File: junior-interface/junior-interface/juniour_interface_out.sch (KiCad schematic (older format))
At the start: 9 parts, among them IC6 NE565, IC7 LM311, IC8 LM311, J3 DB25_Female, T1 BC547

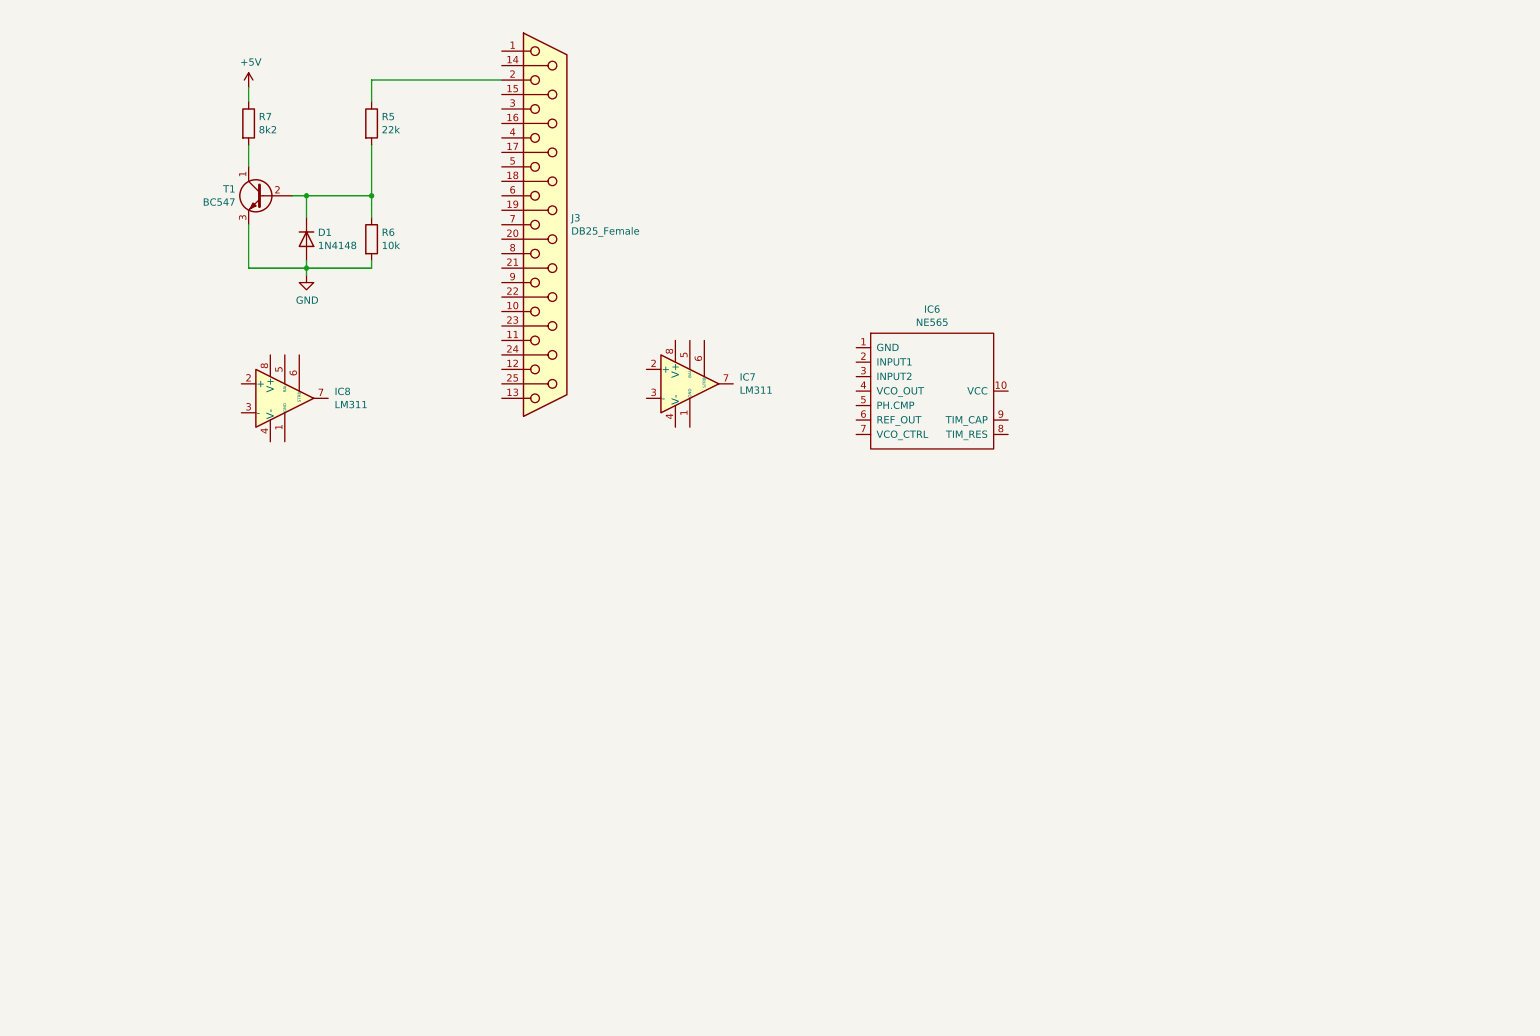
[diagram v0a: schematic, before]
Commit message: junior interface schema
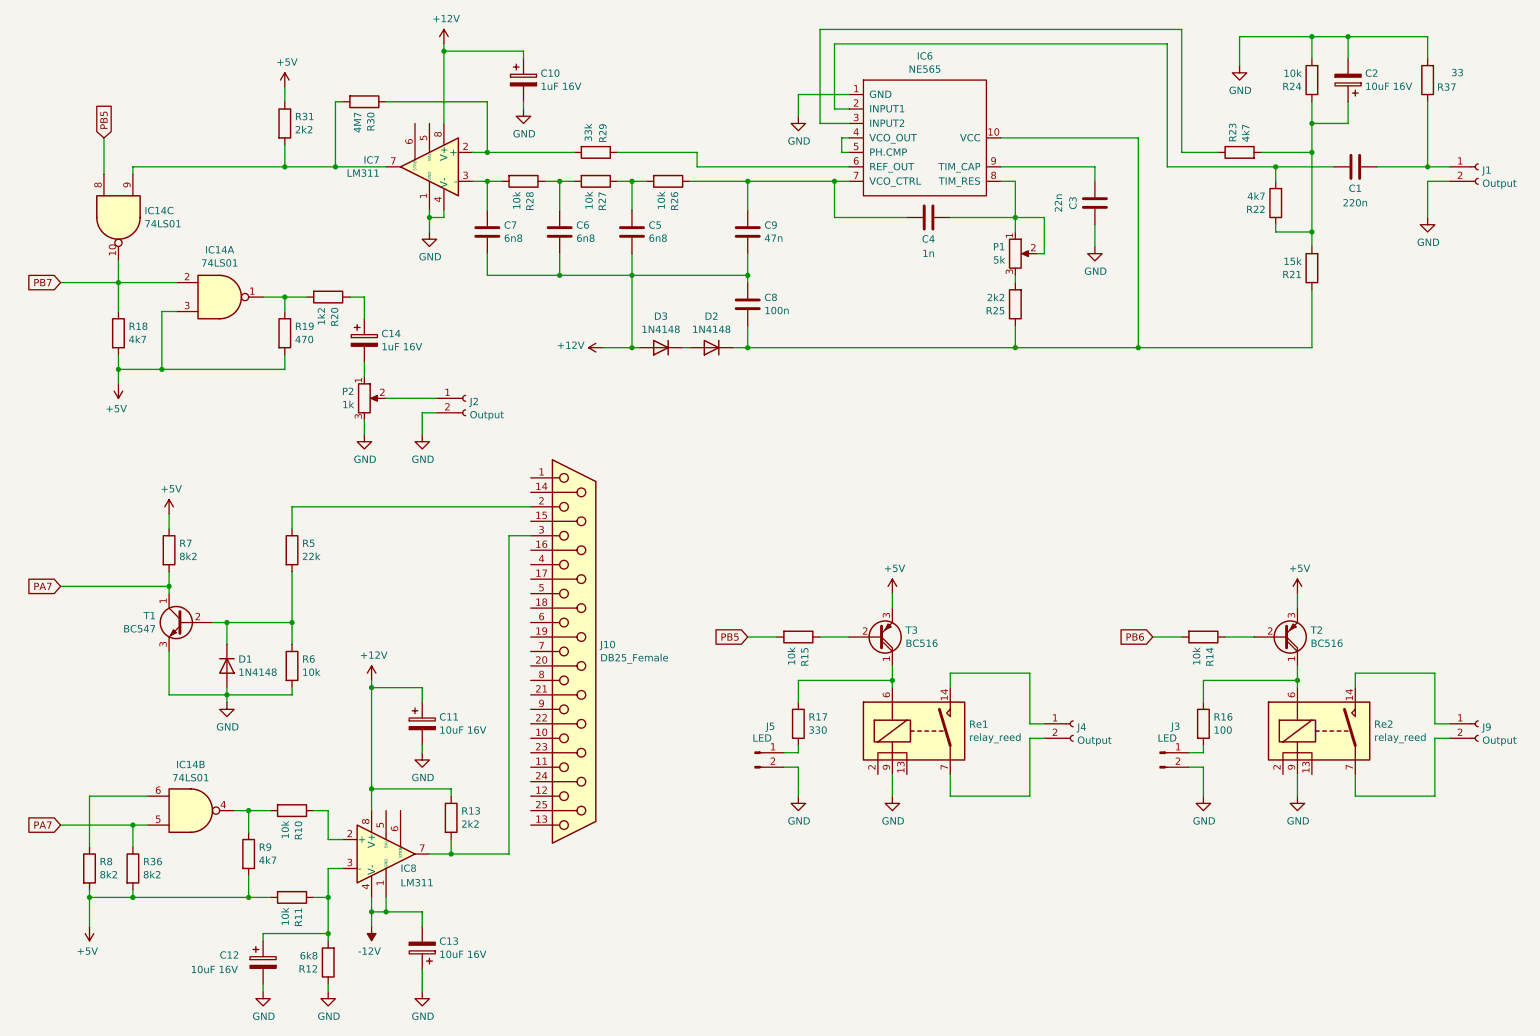
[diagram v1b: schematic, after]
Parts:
- added C1: 220n, elektor:CAP-3, symbol Device:C
- added C10, C14: 1uF 16V, elektor:CAP-POL-3, symbol Device:CP
- added C11, C12, C13, C2: 10uF 16V, elektor:CAP-POL-3, symbol Device:CP
- added C3: 22n, elektor:CAP-3, symbol Device:C
- added C4: 1n, elektor:CAP-3, symbol Device:C
- added C5, C6, C7: 6n8, elektor:CAP-3, symbol Device:C
- added C8: 100n, elektor:CAP-3, symbol Device:C
- added C9: 47n, elektor:CAP-3, symbol Device:C
- added D2, D3: 1N4148, elektor:Diod-4, symbol Device:D
- added IC14: 74LS01, symbol 74xx:74LS01
- added J1, J2, J4, J9: Output, elektor:RCA_CI, symbol Connector:Conn_01x02_Female
- added J3, J5: LED, symbol Connector:Conn_01x02_Male
- added P1: 5k, Potentiometers:Potentiometer_Trimmer_Bourns_3005, symbol Device:R_POT
- added P2: 1k, Potentiometers:Potentiometer_Trimmer_ACP_CA9v_Horizontal_Px10.0mm_Py5.0mm, symbol Device:R_POT
- added R10, R11, R14, R15, R24, R26, R27, R28: 10k, elektor:Res-5, symbol Device:R
- added R12: 6k8, elektor:Res-5, symbol Device:R
- added R13, R25, R31: 2k2, elektor:Res-5, symbol Device:R
- added R16: 100, elektor:Res-5, symbol Device:R
- added R17: 330, elektor:Res-5, symbol Device:R
- added R18, R22, R23, R9: 4k7, elektor:Res-5, symbol Device:R
- added R19: 470, elektor:Res-5, symbol Device:R
- added R20: 1k2, elektor:Res-5, symbol Device:R
- added R21: 15k, elektor:Res-5, symbol Device:R
- added R29: 33k, elektor:Res-5, symbol Device:R
- added R30: 4M7, elektor:Res-5, symbol Device:R
- added R36, R8: 8k2, elektor:Res-5, symbol Device:R
- added R37: 33, elektor:Res-5, symbol Device:R
- added Re1, Re2: relay_reed, elektor:DIL-14, symbol junior_computer:relay_reed
- added T2, T3: BC516, TO_SOT_Packages_THT:TO-92_Molded_Wide, symbol Transistor_BJT:BC516
- J10: renamed from J3; footprint (none) -> elektor:DB25-F-CI
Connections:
- net +5V: now also IC14.3, R11.2, R18.2, R19.2, R31.1, R36.2, R8.2, R9.2, T2.3 (E), T3.3 (E)
- net GND: now also IC6.1 (GND), IC7.1 (GND), IC7.4 (V-), C10.2, C11.2, C12.2, C13.1, C2.2, C3.2, J1.2 (Pin_2), J2.2 (Pin_2), J3.2 (Pin_2), J5.2 (Pin_2), P2.3, R12.1, R24.2, R37.2, Re1.9, Re2.9
- net at IC7.2 (+): now also R29.2, R30.1
- net at IC7.3 (-): now also C7.1, R28.2
- net at IC7.7: now also IC14.9, R30.2, R31.2
- net +12V: now reaches IC7.8 (V+)
- net +12V: now also IC8.8 (V+), C10.1, C11.1, C5.2, C6.2, C7.2, C8.1, C9.2, D3.2 (A), R13.1
- net -12V: now reaches IC8.1 (GND)
- net -12V: now also IC8.4 (V-), C13.2
- net at IC8.2 (+): now also R10.1
- net at IC8.3 (-): now also C12.1, R11.1, R12.2
- net at IC8.7: now also J10.3, R13.2
- net at IC6.10 (VCC): now also C8.2, D2.1 (K), R21.1, R25.1
- net at IC6.2 (INPUT1): now also C1.1, R22.2
- net at IC6.3 (INPUT2): now also R23.1
- net at IC6.4 (VCO_OUT): now also IC6.5 (PH.CMP)
- net at IC6.6 (REF_OUT): now also R29.1
- net at IC6.7 (VCO_CTRL): now also C4.1, C9.1, R26.1
- net at IC6.8 (TIM_RES): now also C4.2, P1.1, P1.2
- net at IC6.9 (TIM_CAP): now also C3.1
- net PA7: now reaches R7.2, T1.1 (C)
- net PA7: now also IC14.5, R36.1
- new net: IC14.4, R10.2, R9.1
- new net: IC14.6, R8.1
- new net: R17.1, Re1.6, T3.1 (C)
- new net: R15.1, T3.2 (B)
- new net: J4.1 (Pin_1), Re1.14
- new net: J4.2 (Pin_2), Re1.7
- new net: J5.1 (Pin_1), R17.2
- new net: R16.1, Re2.6, T2.1 (C)
- new net: R14.1, T2.2 (B)
- new net: J9.1 (Pin_1), Re2.14
- new net: J9.2 (Pin_2), Re2.7
- new net: J3.1 (Pin_1), R16.2
- new net: IC14.1, R19.1, R20.2
- new net: C14.1, R20.1
- new net: C14.2, P2.1
- new net: J2.1 (Pin_1), P2.2
- new net: C6.1, R27.2, R28.1
- new net: C5.1, R26.2, R27.1
- new net: D2.2 (A), D3.1 (K)
- new net: P1.3, R25.2
- new net: C2.1, R21.2, R22.1, R23.2, R24.1
- new net: C1.2, J1.1 (Pin_1), R37.1
- new net PB5: IC14.8, R15.2
- new net PB6: R14.2
- new net PB7: IC14.10, IC14.2, R18.1
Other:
- moved on the sheet: D1, IC6, IC7, IC8, J10, R5, R6, R7, T1

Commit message: junior interface routage
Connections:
- net GND: now also P2.1; no longer P2.3
- net at C14.2: now also P2.3; no longer P2.1
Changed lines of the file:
@@
 F 3 "~" H 3050 3200 50  0001 C CNN
 	1    3050 3200
-	1    0    0    -1
+	1    0    0    1
 $EndComp
 $Comp

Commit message: junior interface routage
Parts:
- J1, J2, J4, J9: footprint elektor:RCA_CI -> elektor:RCA_CI_1
- J10: footprint elektor:DB25-F-CI -> Connectors_DSub:DSUB-25_Female_Horizontal_Pitch2.77x2.84mm_EdgePinOffset9.90mm_Housed_MountingHolesOffset11.32mm
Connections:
- net GND: now also J10.7
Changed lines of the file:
@@
 F 0 "J10" H 4680 4996 50  0000 L CNN
 F 1 "DB25_Female" H 4680 4905 50  0000 L CNN
-F 2 "elektor:DB25-F-CI" H 4500 4950 50  0001 C CNN
+F 2 "Connectors_DSub:DSUB-25_Female_Horizontal_Pitch2.77x2.84mm_EdgePinOffset9.90mm_Housed_MountingHolesOffset11.32mm" H 4500 4950 50  0001 C CNN
 F 3 " ~" H 4500 4950 50  0001 C CNN
 	1    4500 4950
@@
 F 0 "J4" H 7978 5426 50  0000 L CNN
 F 1 "Output" H 7978 5335 50  0000 L CNN
-F 2 "elektor:RCA_CI" H 7950 5450 50  0001 C CNN
+F 2 "elektor:RCA_CI_1" H 7950 5450 50  0001 C CNN
 F 3 "~" H 7950 5450 50  0001 C CNN
 	1    7950 5450
@@
 F 0 "J9" H 10778 5426 50  0000 L CNN
 F 1 "Output" H 10778 5335 50  0000 L CNN
-F 2 "elektor:RCA_CI" H 10750 5450 50  0001 C CNN
+F 2 "elektor:RCA_CI_1" H 10750 5450 50  0001 C CNN
 F 3 "~" H 10750 5450 50  0001 C CNN
 	1    10750 5450
@@
 F 0 "J2" H 3778 3176 50  0000 L CNN
 F 1 "Output" H 3778 3085 50  0000 L CNN
-F 2 "elektor:RCA_CI" H 3750 3200 50  0001 C CNN
+F 2 "elektor:RCA_CI_1" H 3750 3200 50  0001 C CNN
 F 3 "~" H 3750 3200 50  0001 C CNN
 	1    3750 3200
@@
 F 0 "J1" H 10778 1576 50  0000 L CNN
 F 1 "Output" H 10778 1485 50  0000 L CNN
-F 2 "elektor:RCA_CI" H 10750 1600 50  0001 C CNN
+F 2 "elektor:RCA_CI_1" H 10750 1600 50  0001 C CNN
 F 3 "~" H 10750 1600 50  0001 C CNN
 	1    10750 1600
@@
 Wire Wire Line
 	10400 1700 10400 1950
+$Comp
+L power:GND #PWR0190
+U 1 1 5F9AB08B
+P 3900 5050
+F 0 "#PWR0190" H 3900 4800 50  0001 C CNN
+F 1 "GND" H 3905 4877 50  0000 C CNN
+F 2 "" H 3900 5050 50  0001 C CNN
+F 3 "" H 3900 5050 50  0001 C CNN
+	1    3900 5050
+	1    0    0    -1
+$EndComp
+Wire Wire Line
+	4200 4950 3900 4950
+Wire Wire Line
+	3900 4950 3900 5050
 $EndSCHEMATC

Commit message: junior interface routage
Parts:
- removed J3, J5: LED, symbol Connector:Conn_01x02_Male
- added J24: P, elektor:PIN, symbol Connector:Conn_01x01_Male
- added J25: Q, elektor:PIN, symbol Connector:Conn_01x01_Male
- added J26: D4, elektor:PIN, symbol Connector:Conn_01x01_Male
- added J27: (no value), elektor:PIN, symbol Connector:Conn_01x01_Male
- added J28: D5, elektor:PIN, symbol Connector:Conn_01x01_Male
- added J29: Conn_01x06_Male, Pin_Headers:Pin_Header_Straight_1x06_Pitch2.54mm, symbol Connector:Conn_01x06_Male
- R16: renamed from R17; value 330 -> 100
- R17: renamed from R16; value 100 -> 330
- renumbered R15 to R14, R14 to R15, T3 to T2, T2 to T3
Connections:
- net GND: now also Re1.13, Re1.2, Re2.13, Re2.2, J27.1 (Pin_1)
- net PA7: now also J24.1 (Pin_1)
- net PB5: now also R15.2; no longer R14.2
- net PB6: now also R14.2; no longer R15.2
- net at C4.2, IC6.8 (TIM_RES), P1.2: now also P1.3; no longer P1.1
- net at IC14.6, R8.1: now also J25.1 (Pin_1)
- net at R16.2: now also J26.1 (Pin_1)
- net at R17.2: now also J28.1 (Pin_1)
- net at R25.2: now also P1.1; no longer P1.3
- net at J10.1: now also J29.1 (Pin_1)
- net at J10.10: now also J29.6 (Pin_6)
- net at J10.20 (P20): now also J29.5 (Pin_5)
- net at J10.4: now also J29.2 (Pin_2)
- net at J10.5: now also J29.3 (Pin_3)
- net at J10.6: now also J29.4 (Pin_4)
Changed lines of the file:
@@
 PA7
 Wire Wire Line
-	950  4500 1700 4500
+	950  4500 1150 4500
 Connection ~ 1700 4500
 Wire Wire Line
@@
 	2350 7250 2350 7300
 $Comp
-L Transistor_BJT:BC516 T3
+L Transistor_BJT:BC516 T2
 U 1 1 5F9A5A99
 P 6600 4850
-F 0 "T3" H 6791 4804 50  0000 L CNN
+F 0 "T2" H 6791 4804 50  0000 L CNN
 F 1 "BC516" H 6791 4895 50  0000 L CNN
 F 2 "TO_SOT_Packages_THT:TO-92_Molded_Wide" H 6800 4775 50  0001 L CIN
@@
 	1    0    0    1
 $EndComp
-Text GLabel 5700 4850 0    50   Input ~ 0
+Text GLabel 8500 4850 0    50   Input ~ 0
 PB5
 $Comp
-L Device:R R15
+L Device:R R14
 U 1 1 5F9A6423
 P 6050 4850
-F 0 "R15" H 6120 4896 50  0000 L CNN
+F 0 "R14" H 6120 4896 50  0000 L CNN
 F 1 "10k" H 6120 4805 50  0000 L CNN
 F 2 "elektor:Res-5" V 5980 4850 50  0001 C CNN
@@
 $EndComp
 Wire Wire Line
-	6700 5800 6700 5950
-$Comp
-L Device:R R17
+	6700 5800 6700 5850
+$Comp
+L Device:R R16
 U 1 1 5F9B5236
 P 6050 5450
-F 0 "R17" H 6120 5496 50  0000 L CNN
-F 1 "330" H 6120 5405 50  0000 L CNN
+F 0 "R16" H 6120 5496 50  0000 L CNN
+F 1 "100" H 6120 5405 50  0000 L CNN
 F 2 "elektor:Res-5" V 5980 5450 50  0001 C CNN
 F 3 "~" H 6050 5450 50  0001 C CNN
@@
 $EndComp
 $Comp
-L Connector:Conn_01x02_Male J5
-U 1 1 5F9B574B
-P 5750 5650
-F 0 "J5" H 5858 5831 50  0000 C CNN
-F 1 "LED" H 5800 5750 50  0000 C CNN
-F 2 "" H 5750 5650 50  0001 C CNN
-F 3 "~" H 5750 5650 50  0001 C CNN
-	1    5750 5650
-	1    0    0    -1
-$EndComp
-$Comp
 L power:GND #PWR0165
 U 1 1 5F9B63FC
-P 6050 5950
-F 0 "#PWR0165" H 6050 5700 50  0001 C CNN
-F 1 "GND" H 6055 5777 50  0000 C CNN
-F 2 "" H 6050 5950 50  0001 C CNN
-F 3 "" H 6050 5950 50  0001 C CNN
-	1    6050 5950
-	1    0    0    -1
-$EndComp
-Wire Wire Line
-	5950 5750 6050 5750
-Wire Wire Line
-	6050 5750 6050 5950
+P 6050 6150
+F 0 "#PWR0165" H 6050 5900 50  0001 C CNN
+F 1 "GND" H 6055 5977 50  0000 C CNN
+F 2 "" H 6050 6150 50  0001 C CNN
+F 3 "" H 6050 6150 50  0001 C CNN
+	1    6050 6150
+	1    0    0    -1
+$EndComp
+Wire Wire Line
+	5950 5950 6050 5950
+Wire Wire Line
+	6050 5950 6050 6150
 Wire Wire Line
 	5950 5650 6050 5650
@@
 	6700 5150 6700 5200
 $Comp
-L Transistor_BJT:BC516 T2
+L Transistor_BJT:BC516 T3
 U 1 1 5F9C15AB
 P 9400 4850
-F 0 "T2" H 9591 4804 50  0000 L CNN
+F 0 "T3" H 9591 4804 50  0000 L CNN
 F 1 "BC516" H 9591 4895 50  0000 L CNN
 F 2 "TO_SOT_Packages_THT:TO-92_Molded_Wide" H 9600 4775 50  0001 L CIN
@@
 	1    0    0    1
 $EndComp
-Text GLabel 8500 4850 0    50   Input ~ 0
+Text GLabel 5700 4850 0    50   Input ~ 0
 PB6
 $Comp
-L Device:R R14
+L Device:R R15
 U 1 1 5F9C15B6
 P 8850 4850
-F 0 "R14" H 8920 4896 50  0000 L CNN
+F 0 "R15" H 8920 4896 50  0000 L CNN
 F 1 "10k" H 8920 4805 50  0000 L CNN
 F 2 "elektor:Res-5" V 8780 4850 50  0001 C CNN
@@
 $EndComp
 Wire Wire Line
-	9500 5800 9500 5950
-$Comp
-L Device:R R16
+	9500 5800 9500 5850
+$Comp
+L Device:R R17
 U 1 1 5F9C15F5
 P 8850 5450
-F 0 "R16" H 8920 5496 50  0000 L CNN
-F 1 "100" H 8920 5405 50  0000 L CNN
+F 0 "R17" H 8920 5496 50  0000 L CNN
+F 1 "330" H 8920 5405 50  0000 L CNN
 F 2 "elektor:Res-5" V 8780 5450 50  0001 C CNN
 F 3 "~" H 8850 5450 50  0001 C CNN
 	1    8850 5450
-	1    0    0    -1
-$EndComp
-$Comp
-L Connector:Conn_01x02_Male J3
-U 1 1 5F9C15FF
-P 8550 5650
-F 0 "J3" H 8658 5831 50  0000 C CNN
-F 1 "LED" H 8600 5750 50  0000 C CNN
-F 2 "" H 8550 5650 50  0001 C CNN
-F 3 "~" H 8550 5650 50  0001 C CNN
-	1    8550 5650
 	1    0    0    -1
 $EndComp
@@
 F 3 "~" H 7550 2200 50  0001 C CNN
 	1    7550 2200
-	1    0    0    -1
+	1    0    0    1
 $EndComp
 $Comp
@@
 Wire Wire Line
 	3900 4950 3900 5050
+Wire Wire Line
+	6600 5800 6600 5850
+Wire Wire Line
+	6600 5850 6700 5850
+Connection ~ 6700 5850
+Wire Wire Line
+	6700 5850 6700 5950
+Wire Wire Line
+	6700 5850 6800 5850
+Wire Wire Line
+	6800 5850 6800 5800
+Wire Wire Line
+	9400 5800 9400 5850
+Wire Wire Line
+	9400 5850 9500 5850
+Connection ~ 9500 5850
+Wire Wire Line
+	9500 5850 9500 5950
+Wire Wire Line
+	9600 5850 9600 5800
+Wire Wire Line
+	9500 5850 9600 5850
+$Comp
+L Connector:Conn_01x01_Male J?
+U 1 1 5FCE8E8C
+P 5750 5650
+AR Path="/5F9396FE/5FCE8E8C" Ref="J?"  Part="1"
+AR Path="/5F939FEF/5FCE8E8C" Ref="J26"  Part="1"
+F 0 "J26" V 5650 5700 50  0000 R CNN
+F 1 "D4" V 5813 5562 50  0000 R CNN
+F 2 "elektor:PIN" H 5750 5650 50  0001 C CNN
+F 3 "~" H 5750 5650 50  0001 C CNN
+	1    5750 5650
+	1    0    0    -1
+$EndComp
+$Comp
+L Connector:Conn_01x01_Male J?
+U 1 1 5FCF6F9E
+P 5750 5950
+AR Path="/5F9396FE/5FCF6F9E" Ref="J?"  Part="1"
+AR Path="/5F939FEF/5FCF6F9E" Ref="J27"  Part="1"
+F 0 "J27" V 5650 6000 50  0000 R CNN
+F 1 " " V 5813 5862 50  0000 R CNN
+F 2 "elektor:PIN" H 5750 5950 50  0001 C CNN
+F 3 "~" H 5750 5950 50  0001 C CNN
+	1    5750 5950
+	1    0    0    -1
+$EndComp
+$Comp
+L Connector:Conn_01x01_Male J?
+U 1 1 5FD04FCB
+P 8550 5650
+AR Path="/5F9396FE/5FD04FCB" Ref="J?"  Part="1"
+AR Path="/5F939FEF/5FD04FCB" Ref="J28"  Part="1"
+F 0 "J28" V 8450 5700 50  0000 R CNN
+F 1 "D5" V 8613 5562 50  0000 R CNN
+F 2 "elektor:PIN" H 8550 5650 50  0001 C CNN
+F 3 "~" H 8550 5650 50  0001 C CNN
+	1    8550 5650
+	1    0    0    -1
+$EndComp
+$Comp
+L Connector:Conn_01x01_Male J?
+U 1 1 5FD13D36
+P 1150 5250
+AR Path="/5F9396FE/5FD13D36" Ref="J?"  Part="1"
+AR Path="/5F939FEF/5FD13D36" Ref="J24"  Part="1"
+F 0 "J24" V 1050 5300 50  0000 R CNN
+F 1 "P" V 1213 5162 50  0000 R CNN
+F 2 "elektor:PIN" H 1150 5250 50  0001 C CNN
+F 3 "~" H 1150 5250 50  0001 C CNN
+	1    1150 5250
+	0    -1   -1   0
+$EndComp
+$Comp
+L Connector:Conn_01x01_Male J?
+U 1 1 5FD21EDB
+P 1150 5550
+AR Path="/5F9396FE/5FD21EDB" Ref="J?"  Part="1"
+AR Path="/5F939FEF/5FD21EDB" Ref="J25"  Part="1"
+F 0 "J25" V 1050 5600 50  0000 R CNN
+F 1 " Q" V 1213 5462 50  0000 R CNN
+F 2 "elektor:PIN" H 1150 5550 50  0001 C CNN
+F 3 "~" H 1150 5550 50  0001 C CNN
+	1    1150 5550
+	0    1    1    0
+$EndComp
+Wire Wire Line
+	1150 5050 1150 4500
+Connection ~ 1150 4500
+Wire Wire Line
+	1150 4500 1700 4500
+Wire Wire Line
+	1150 5950 1150 5750
+Connection ~ 1150 5950
+$Comp
+L Connector:Conn_01x06_Male J29
+U 1 1 5FD8DDA2
+P 3450 4400
+F 0 "J29" H 3558 4781 50  0000 C CNN
+F 1 "Conn_01x06_Male" H 3400 4700 50  0000 C CNN
+F 2 "Pin_Headers:Pin_Header_Straight_1x06_Pitch2.54mm" H 3450 4400 50  0001 C CNN
+F 3 "~" H 3450 4400 50  0001 C CNN
+	1    3450 4400
+	1    0    0    -1
+$EndComp
+Wire Wire Line
+	3650 4200 3800 4200
+Wire Wire Line
+	3800 4200 3800 3750
+Wire Wire Line
+	3800 3750 4200 3750
+Wire Wire Line
+	4200 4350 3950 4350
+Wire Wire Line
+	3950 4350 3950 4300
+Wire Wire Line
+	3950 4300 3650 4300
+Wire Wire Line
+	4200 4550 3900 4550
+Wire Wire Line
+	3900 4550 3900 4400
+Wire Wire Line
+	3900 4400 3650 4400
+Wire Wire Line
+	4200 4750 3850 4750
+Wire Wire Line
+	3850 4750 3850 4500
+Wire Wire Line
+	3850 4500 3650 4500
+Wire Wire Line
+	4200 5050 4000 5050
+Wire Wire Line
+	4000 5050 4000 4800
+Wire Wire Line
+	4000 4800 3800 4800
+Wire Wire Line
+	3800 4800 3800 4600
+Wire Wire Line
+	3800 4600 3650 4600
+Wire Wire Line
+	4200 5550 4000 5550
+Wire Wire Line
+	4000 5550 4000 5350
+Wire Wire Line
+	4000 5350 3750 5350
+Wire Wire Line
+	3750 5350 3750 4700
+Wire Wire Line
+	3750 4700 3650 4700
 $EndSCHEMATC

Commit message: junior interface routage complet
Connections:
- net PA7 renamed OPA7
- net OPA7: no longer IC14.5, R36.1
- net PB5 renamed OPB5
- net PB6 renamed OPB6
- net PB7 renamed OPB7
- new net OPB0: IC14.5, R36.1
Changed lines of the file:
@@
 	2550 3950 2550 4100
 Text GLabel 950  4500 0    50   Input ~ 0
-PA7
+OPA7
 Wire Wire Line
 	950  4500 1150 4500
@@
 	1150 5950 1150 6300
 Text GLabel 950  6150 0    50   Input ~ 0
-PA7
+OPB0
 Wire Wire Line
 	950  6150 1450 6150
@@
 $EndComp
 Text GLabel 8500 4850 0    50   Input ~ 0
-PB5
+OPB5
 $Comp
 L Device:R R14
@@
 $EndComp
 Text GLabel 5700 4850 0    50   Input ~ 0
-PB6
+OPB6
 $Comp
 L Device:R R15
@@
 	9500 5150 9500 5200
 Text GLabel 950  2400 0    50   Input ~ 0
-PB7
+OPB7
 $Comp
 L Device:R R18
@@
 	3050 3350 3050 3450
 Text GLabel 1250 1400 1    50   Input ~ 0
-PB5
+OPB5
 Wire Wire Line
 	1250 1400 1250 1650
